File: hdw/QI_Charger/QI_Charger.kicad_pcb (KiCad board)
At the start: 2 copper layers, 150 x 50 mm, 305 parts, among them J1001 USB_B_Mini, J1301 PAD, J1302 PAD, J201 +12V IN, J401 PICKIT3, Q201 IPC100N04S51R7ATMA1, Q202 IPC100N04S51R7ATMA1, Q401 BSS214NW, SW401 MRST, SW801 Cap_Touch, SW802 Cap_Touch, U1001 LT6700-1-S6, U1002 FT234XD, U1003 74LVC1G06, U1004 TPD3S014DBVR, U1101 74LVC1G06, U1102 74LVC1G07, U1103 74LVC1G07, U1104 74LVC1G06, U1105 74LVC1G07, U1106 74LVC1G06, U1107 74LVC1G06, U1108 74LVC1G06, U1109 74LVC1G06, U1201 LM73-1, U1202 LM73-1, U1203 LM73-1, U1301 INA138, U1302 NXQ1TXH5_101J, U1401 74LVC1G14, U1402 74LVC1G14, U1403 74LVC1G17, U201 LTC4365DDB, U202 INA138, U301 TPS62130, U302 74LVC1G17, U501 74LVC1G17, U502 74LVC1G17, U503 PIC18F27K40T-I_ML, U601 OPA340NA, U602 OPA340NA, U603 OPA340NA, U604 OPA340NA, U701 SSD1306, U801 AT42QT1010-TSHR, U802 AT42QT1010-TSHR, U901 ISO7321C, Y1301 32.768kHz, Y501 16MHz

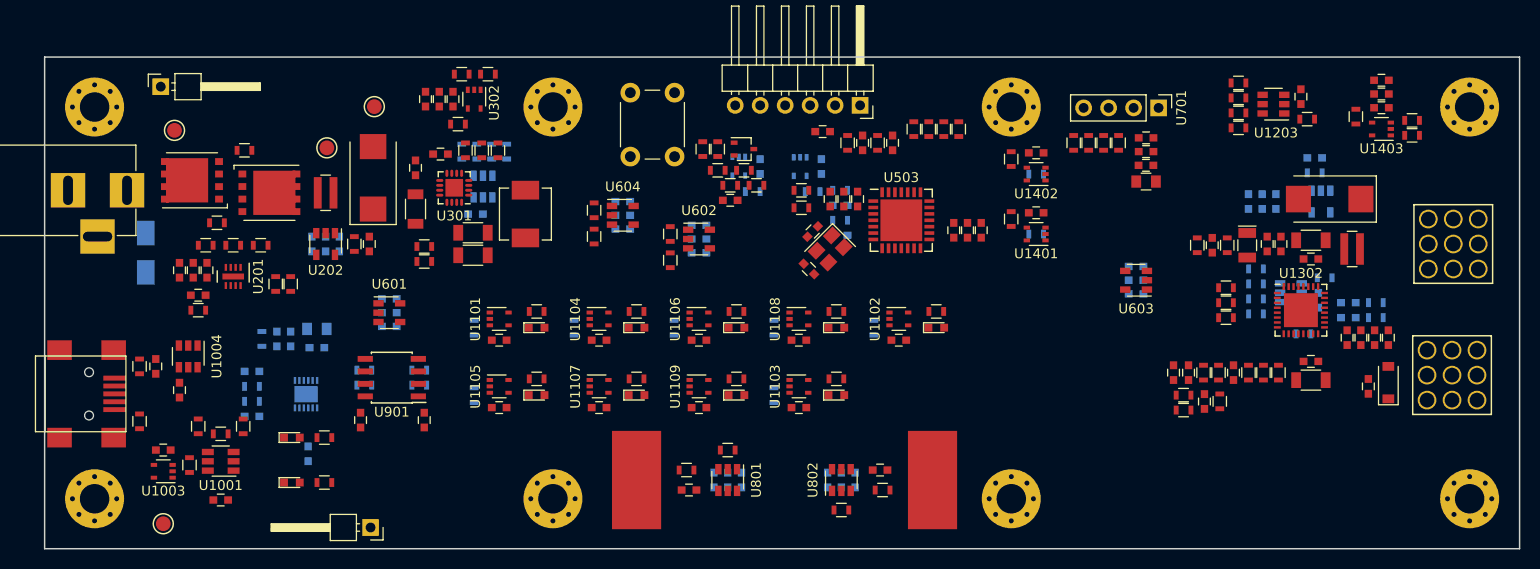
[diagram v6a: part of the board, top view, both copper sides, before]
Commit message: rearranged some parts, got rid of PIC crystal
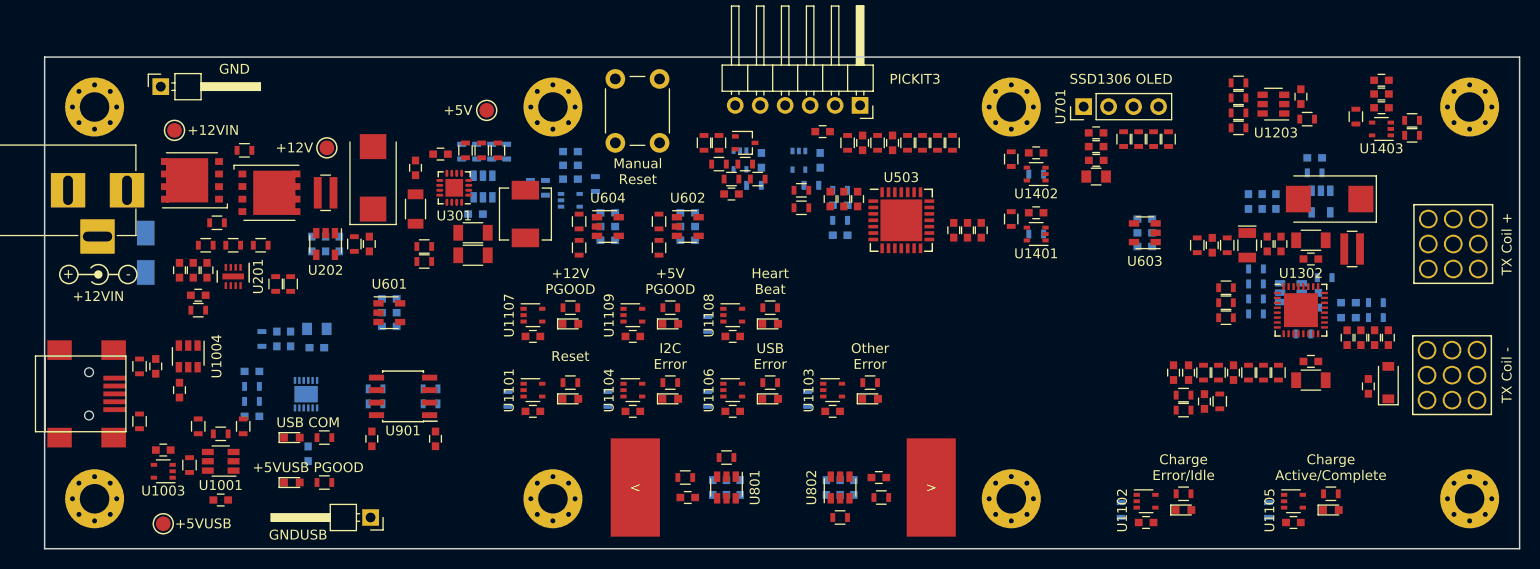
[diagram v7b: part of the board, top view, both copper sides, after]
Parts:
- removed C509, C510: 18pF, Capacitors_SMD:C_0603
- removed Y501: 16MHz, Crystals:Crystal_SMD_TXC_7M-4pin_3.2x2.5mm
- added REF**: Symbol_Barrel_Polarity, Symbols:Symbol_Barrel_Polarity, F.Cu at (44.7, 68.6)
- C304, C305, C306, R304, R305, R308, U302: moved to B.Cu
- moved R1108 81.6 mm to (163.7, 92.5)
- moved C1105 81.6 mm to (166.2, 93.7)
- moved D1105 81.6 mm to (170.1, 92.5)
- moved R1110 81.6 mm to (170.1, 90.8)
- moved U1105 81.6 mm to (166.2, 91.6)
- moved D1102 31.2 mm to (155.1, 92.5)
- moved R1102 31.2 mm to (148.7, 92.5)
- moved R1105 31.2 mm to (155.1, 90.8)
- moved C1102 31.2 mm to (151.3, 93.7)
- moved U1102 31.2 mm to (151.3, 91.6)
- moved C304 15.7 mm to (92.7, 56.0), turned to 180 degrees
- moved R308 15.2 mm to (95.2, 59.3), turned to 90 degrees
- moved C305 14.9 mm to (92.7, 57.4), turned to 180 degrees
- moved C306 14.4 mm to (92.7, 58.8), turned to 180 degrees
- moved R305 14.4 mm to (90.2, 59.7), turned to 90 degrees
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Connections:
- U503 pad 6: PIC_OSC1 -> Cap_Touch_Left
- U503 pad 7: PIC_OSC2 -> Cap_Touch_Right
- U503 pad 8: Cap_Touch_Left -> (no net)
- U503 pad 9: Cap_Touch_Right -> (no net)
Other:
- board text added: "+"
- board text added: "+12V"
- board text added: "+12V PGOOD"
- board text added: "+12VIN"
- board text added: "+5V"
- board text added: "+5V PGOOD"
- board text added: "+5VUSB"
- board text added: "+5VUSB PGOOD"
- board text added: "-"
- board text added: "<"
- board text added: ">"
- board text added: "Charge Active/Complete"
- board text added: "Charge Error/Idle"
- board text added: "GND"
- board text added: "GNDUSB"
- board text added: "Heart Beat"
- board text added: "I2C Error"
- board text added: "Manual Reset"
- board text added: "Other Error"
- board text added: "PICKIT3"
- board text added: "Reset"
- board text added: "SSD1306 OLED"
- board text added: "TX Coil +"
- board text added: "TX Coil -"
- board text added: "USB COM"
- board text added: "USB Error"

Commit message: Added design rules, layer setup
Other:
- copper layers 2 -> 4
- net class Default: clearance 0.2 -> 0.127; trace_width 0.25 -> 0.254; via_dia 0.8 -> 0.5588; via_drill 0.4 -> 0.199898
- net class Power added: clearance 0.127, trace_width 0.635, via_dia 0.5588, via_drill 0.199898
- net class Signal added: clearance 0.127, trace_width 0.254, via_dia 0.5588, via_drill 0.199898
- rule trace_clearance: 0.2 -> 0.127
- rule trace_min: 0.2 -> 0.127
- rule via_min_drill: 0.3 -> 0.199898
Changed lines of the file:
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@@
   (page A)
   (layers
-    (0 F.Cu signal)
-    (31 B.Cu signal)
+    (0 F.Cu mixed)
+    (1 In1.Cu mixed)
+    (2 In2.Cu mixed)
+    (31 B.Cu mixed)
     (32 B.Adhes user)
     (33 F.Adhes user)
@@
   )
   (setup
-    (last_trace_width 0.25)
-    (trace_clearance 0.2)
+    (last_trace_width 0.254)
+    (trace_clearance 0.127)
     (zone_clearance 0.508)
     (zone_45_only no)
-    (trace_min 0.2)
+    (trace_min 0.127)
     (segment_width 0.2)
     (edge_width 0.15)
-    (via_size 0.8)
-    (via_drill 0.4)
+    (via_size 0.5588)
+    (via_drill 0.199898)
     (via_min_size 0.4)
-    (via_min_drill 0.3)
+    (via_min_drill 0.199898)
     (uvia_size 0.3)
     (uvia_drill 0.1)
@@
   (net 137 QI_OSC_2)
   (net_class Default "This is the default net class."
-    (clearance 0.2)
-    (trace_width 0.25)
-    (via_dia 0.8)
-    (via_drill 0.4)
+    (clearance 0.127)
+    (trace_width 0.254)
+    (via_dia 0.5588)
+    (via_drill 0.199898)
+    (uvia_dia 0.3)
+    (uvia_drill 0.1)
+  )
+  (net_class Power ""
+    (clearance 0.127)
+    (trace_width 0.635)
+    (via_dia 0.5588)
+    (via_drill 0.199898)
     (uvia_dia 0.3)
     (uvia_drill 0.1)
@@
     (add_net +12Vin)
     (add_net +5V)
-    (add_net +5VADC)
     (add_net +5VP)
     (add_net +5V_USB)
+    (add_net GND)
+    (add_net GNDA)
+    (add_net GND_USB)
+  )
+  (net_class Signal ""
+    (clearance 0.127)
+    (trace_width 0.254)
+    (via_dia 0.5588)
+    (via_drill 0.199898)
+    (uvia_dia 0.3)
+    (uvia_drill 0.1)
+    (add_net +5VADC)
     (add_net /Microcontroller/PIC_I2C_SCL)
     (add_net /Microcontroller/PIC_I2C_SDA)
@@
     (add_net Cap_Touch_Left)
     (add_net Cap_Touch_Right)
-    (add_net GND)
-    (add_net GNDA)
-    (add_net GND_USB)
     (add_net Heartbeat_LED)
     (add_net I2C_Error_LED)
